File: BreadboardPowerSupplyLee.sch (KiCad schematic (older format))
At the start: 16 parts

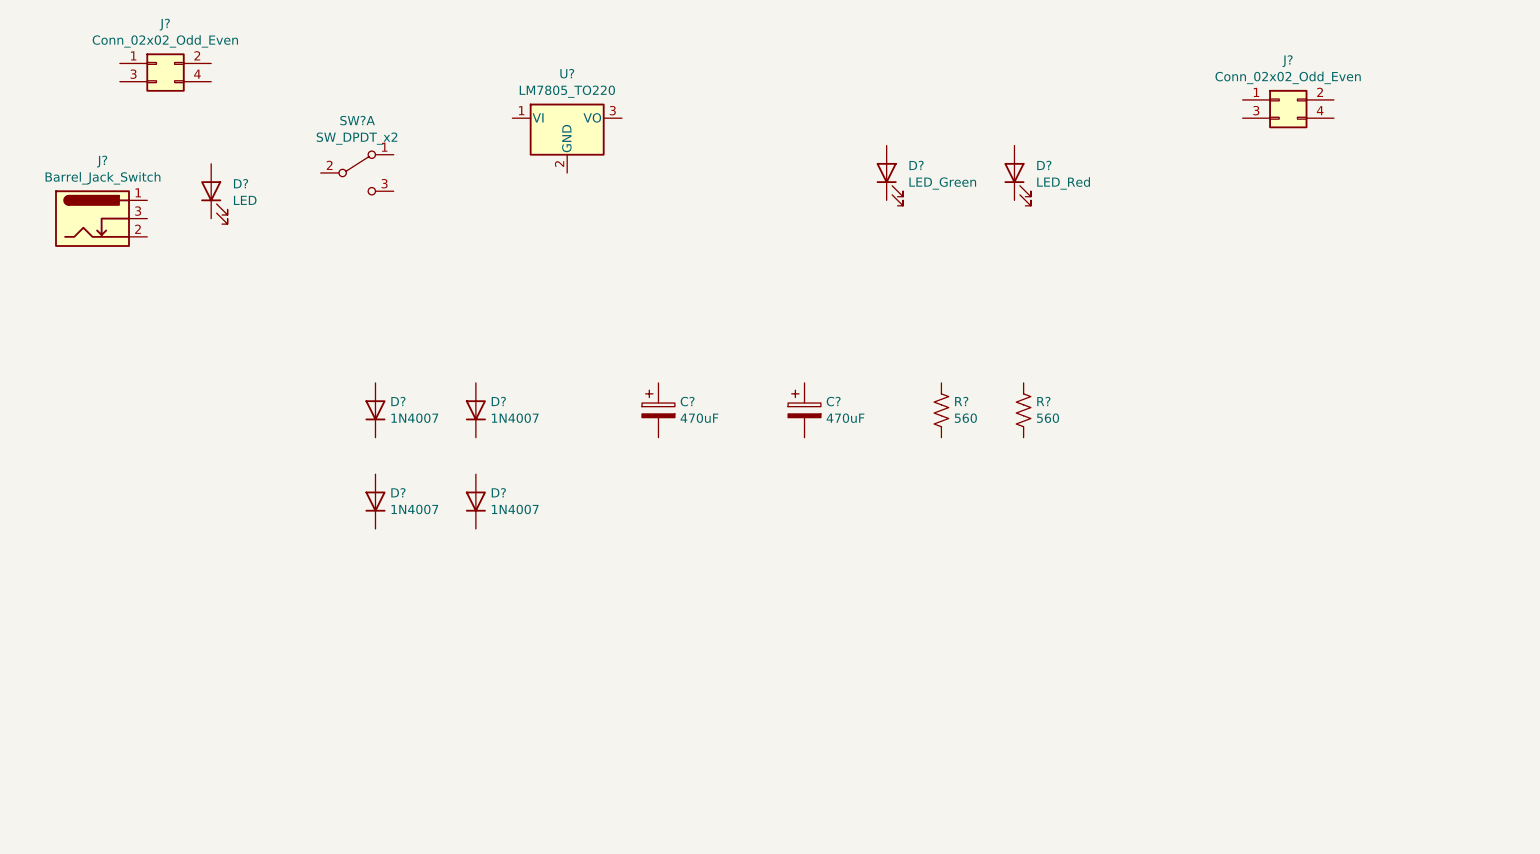
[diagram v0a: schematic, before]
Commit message: Update finish schematic. Start PCB with outline and place J2 and J3.
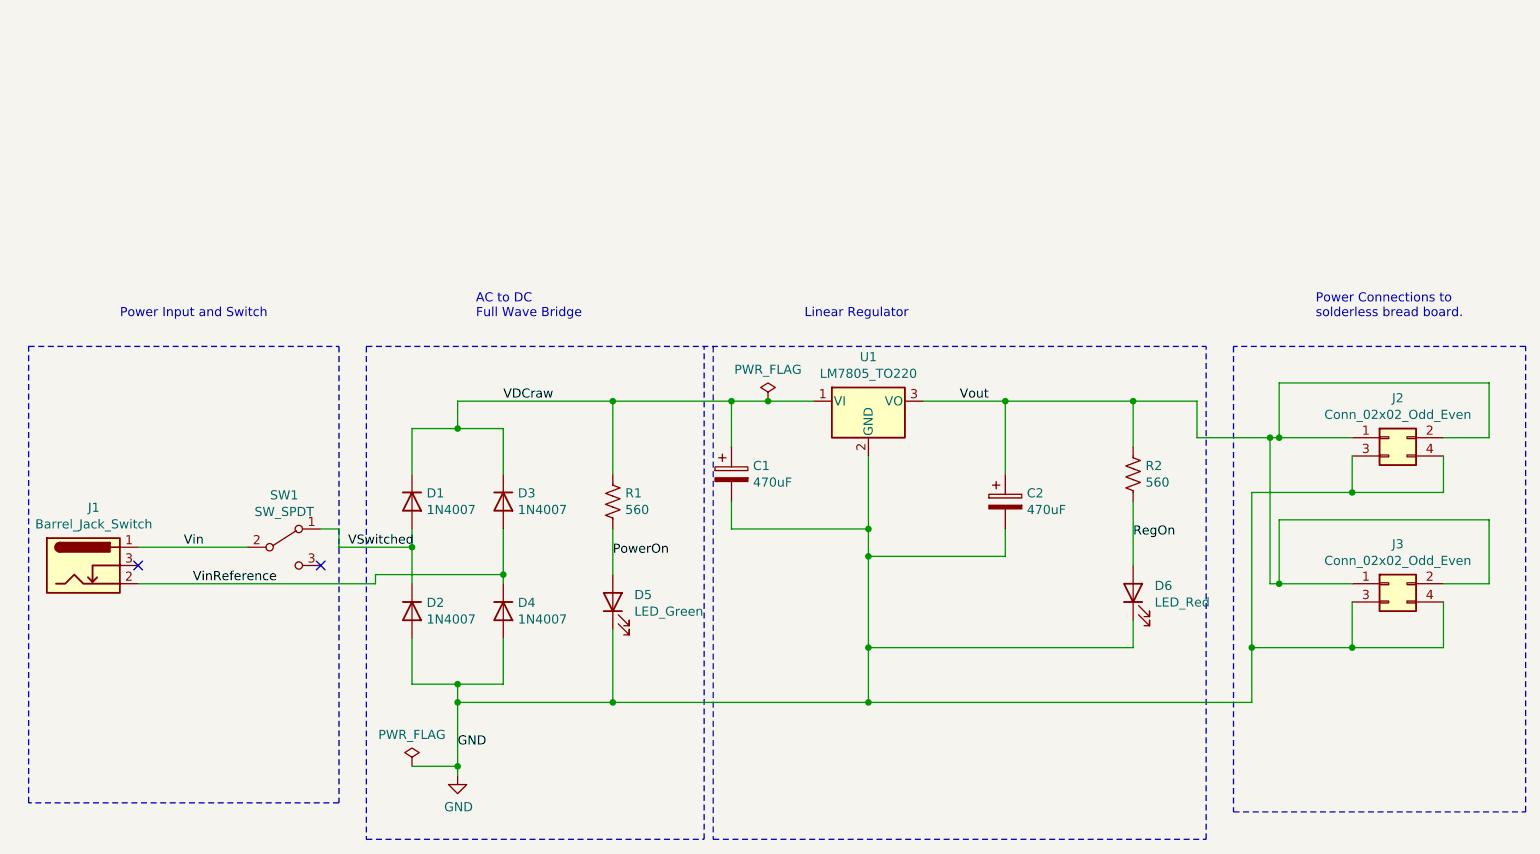
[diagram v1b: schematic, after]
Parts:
- removed D? (x3): 1N4007, symbol Device:D
- removed D?: LED, symbol Device:LED
- removed SW?: SW_DPDT_x2, symbol Switch:SW_DPDT_x2
- added D2, D3, D4: 1N4007, Diode_THT:D_DO-41_SOD81_P10.16mm_Horizontal, symbol Device:D
- added SW1: SW_SPDT, digikey-footprints:Switch_Slide_11.6x4mm_EG1218, symbol Switch:SW_SPDT
- C1: renamed from C?; footprint (none) -> Capacitor_THT:CP_Radial_D10.0mm_P5.00mm
- C2: renamed from C?; footprint (none) -> Capacitor_THT:CP_Radial_D6.3mm_P2.50mm
- D1: renamed from D?; footprint (none) -> Diode_THT:D_DO-41_SOD81_P10.16mm_Horizontal
- D5, D6: renamed from D?; footprint (none) -> LED_THT:LED_D5.0mm
- J1: renamed from J?; footprint (none) -> Connector_BarrelJack:BarrelJack_Horizontal
- J2, J3: renamed from J?; footprint (none) -> Connector_PinHeader_2.54mm:PinHeader_2x02_P2.54mm_Vertical
- R1, R2: renamed from R?; footprint (none) -> Resistor_THT:R_Axial_DIN0207_L6.3mm_D2.5mm_P7.62mm_Horizontal
- gave numbers to parts that had none: 1
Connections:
- net VDCraw: now reaches C1.1
- net VDCraw: now also D1.1 (K), R1.1, U1.1 (VI), D3.1 (K)
- net GND: now reaches C1.2
- net GND: now also C2.2, D5.1 (K), D6.1 (K), J2.3 (Pin_3), J2.4 (Pin_4), J3.3 (Pin_3), J3.4 (Pin_4), U1.2 (GND), D2.2 (A), D4.2 (A)
- net Vout: now reaches C2.1
- net Vout: now also J2.1 (Pin_1), J2.2 (Pin_2), J3.1 (Pin_1), J3.2 (Pin_2), R2.1, U1.3 (VO)
- net PowerOn: now reaches R1.2
- net PowerOn: now also D5.2 (A)
- net RegOn: now reaches R2.2
- net RegOn: now also D6.2 (A)
- net VSwitched: now reaches D1.2 (A)
- net VSwitched: now also D2.1 (K), SW1.1 (A)
- net Vin: now reaches J1.1
- net Vin: now also SW1.2 (B)
- net VinReference: now reaches J1.2
- net VinReference: now also D3.2 (A), D4.1 (K)
- no-connect marks 0 -> 2
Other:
- note added: "AC to DC \nFull Wave Bridge"
- note added: "Linear Regulator"
- note added: "Power Connections to \nsolderless bread board."
- note added: "Power Input and Switch"
- moved on the sheet: C1, C2, D1, D5, D6, J1, J2, J3, R1, R2, U1

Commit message: Add test point for Vcc and GND in schematic and PCB. Make gerbers. Looking good.
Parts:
- added GND: GND, TestPoint:TestPoint_THTPad_2.5x2.5mm_Drill1.2mm, symbol Connector:TestPoint
- added Vcc: Vcc, TestPoint:TestPoint_THTPad_2.5x2.5mm_Drill1.2mm, symbol Connector:TestPoint
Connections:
- net GND: now also GND.1
- net Vout: now also Vcc.1
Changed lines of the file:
@@
 	2950 5000 2950 5100
 Wire Wire Line
-	2950 5100 3800 5100
+	2950 5100 3350 5100
 Wire Wire Line
 	5200 5100 5200 4800
@@
 	6650 3700 6650 3450
 Wire Wire Line
-	6650 3450 5950 3450
+	6650 3450 6450 3450
 Connection ~ 5950 3450
 Wire Wire Line
@@
 Text Notes 7650 3000 0    50   ~ 0
 Power Connections to \nsolderless bread board.
+$Comp
+L Connector:TestPoint GND
+U 1 1 613A17C1
+P 3350 5100
+F 0 "GND" H 3408 5218 50  0000 L CNN
+F 1 "GND" H 3400 5150 50  0000 L CNN
+F 2 "TestPoint:TestPoint_THTPad_2.5x2.5mm_Drill1.2mm" H 3550 5100 50  0001 C CNN
+F 3 "~" H 3550 5100 50  0001 C CNN
+	1    3350 5100
+	1    0    0    -1
+$EndComp
+Connection ~ 3350 5100
+Wire Wire Line
+	3350 5100 3800 5100
+$Comp
+L Connector:TestPoint Vcc
+U 1 1 613A1CE4
+P 6450 3450
+F 0 "Vcc" H 6508 3568 50  0000 L CNN
+F 1 "Vcc" H 6500 3500 50  0000 L CNN
+F 2 "TestPoint:TestPoint_THTPad_2.5x2.5mm_Drill1.2mm" H 6650 3450 50  0001 C CNN
+F 3 "~" H 6650 3450 50  0001 C CNN
+	1    6450 3450
+	1    0    0    -1
+$EndComp
+Connection ~ 6450 3450
+Wire Wire Line
+	6450 3450 5950 3450
 $EndSCHEMATC

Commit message: Change test points to Vcc1 and GND1. Remove backup schematic file.
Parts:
- renumbered GND to GND1, Vcc to Vcc1
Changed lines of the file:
@@
 Power Connections to \nsolderless bread board.
 $Comp
-L Connector:TestPoint GND
+L Connector:TestPoint GND1
 U 1 1 613A17C1
 P 3350 5100
-F 0 "GND" H 3408 5218 50  0000 L CNN
+F 0 "GND1" H 3408 5218 50  0000 L CNN
 F 1 "GND" H 3400 5150 50  0000 L CNN
 F 2 "TestPoint:TestPoint_THTPad_2.5x2.5mm_Drill1.2mm" H 3550 5100 50  0001 C CNN
@@
 	3350 5100 3800 5100
 $Comp
-L Connector:TestPoint Vcc
+L Connector:TestPoint Vcc1
 U 1 1 613A1CE4
 P 6450 3450
-F 0 "Vcc" H 6508 3568 50  0000 L CNN
+F 0 "Vcc1" H 6508 3568 50  0000 L CNN
 F 1 "Vcc" H 6500 3500 50  0000 L CNN
 F 2 "TestPoint:TestPoint_THTPad_2.5x2.5mm_Drill1.2mm" H 6650 3450 50  0001 C CNN
